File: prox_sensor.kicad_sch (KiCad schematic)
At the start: 16 parts, among them J1 +, J10 K, J2 -, J3 A, J4 A, J9 K, U1 BD4840G-TR, U6 NCP718xSN330

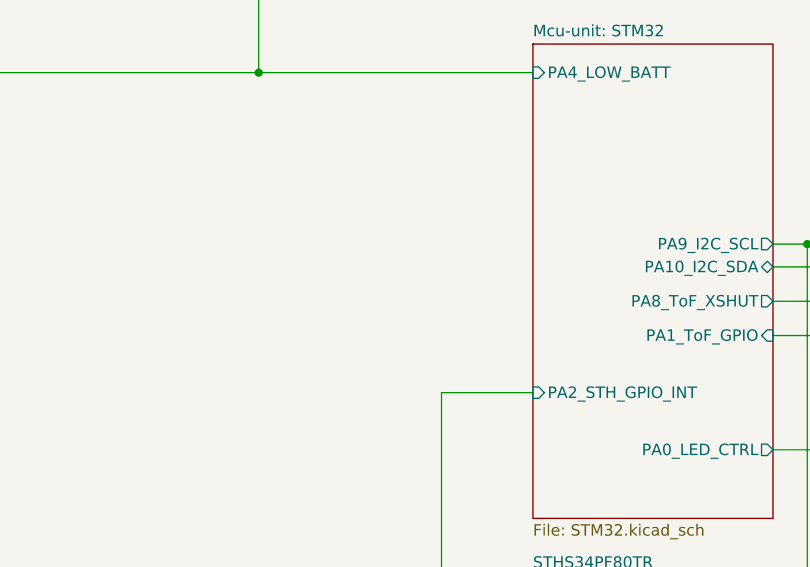
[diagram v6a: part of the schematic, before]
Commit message: Adding power control and extra input, to attach another som
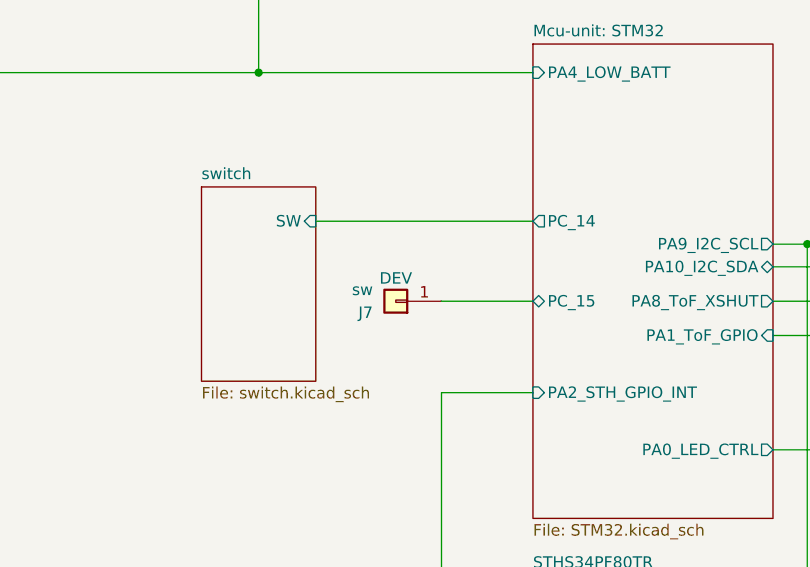
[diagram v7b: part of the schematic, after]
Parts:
- added J7: sw, TestPoint:TestPoint_Pad_D1.0mm, symbol Connector_Generic:Conn_01x01
- U6: LCSC Part # (none) -> C603785
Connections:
- new net Mcu-unit: STM32/PC_15: J7.1 (Pin_1)
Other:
- added sheet switch (switch.kicad_sch)
- sheet Mcu-unit: STM32 ports: added PC_14, PC_15; removed none
